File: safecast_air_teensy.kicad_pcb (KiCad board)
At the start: 2 copper layers, 108 x 69.8 mm, 47 parts, among them P1 CONN_5X2, P10 CONN_5_MOD, P2 CONN_5X2, P3 CONN_5X2, P4 CONN_2X2, P5 CONN_2, P6 CONN_2, P7 CONN_2, P8 CONN_2, P9 CONN_2, U1 GPS, U2 XBEE, U3 LCD, U4 OPENLOG, U5 POLOLU_3V3, U6 TEENSY3.1, U7 R5_BUSSED

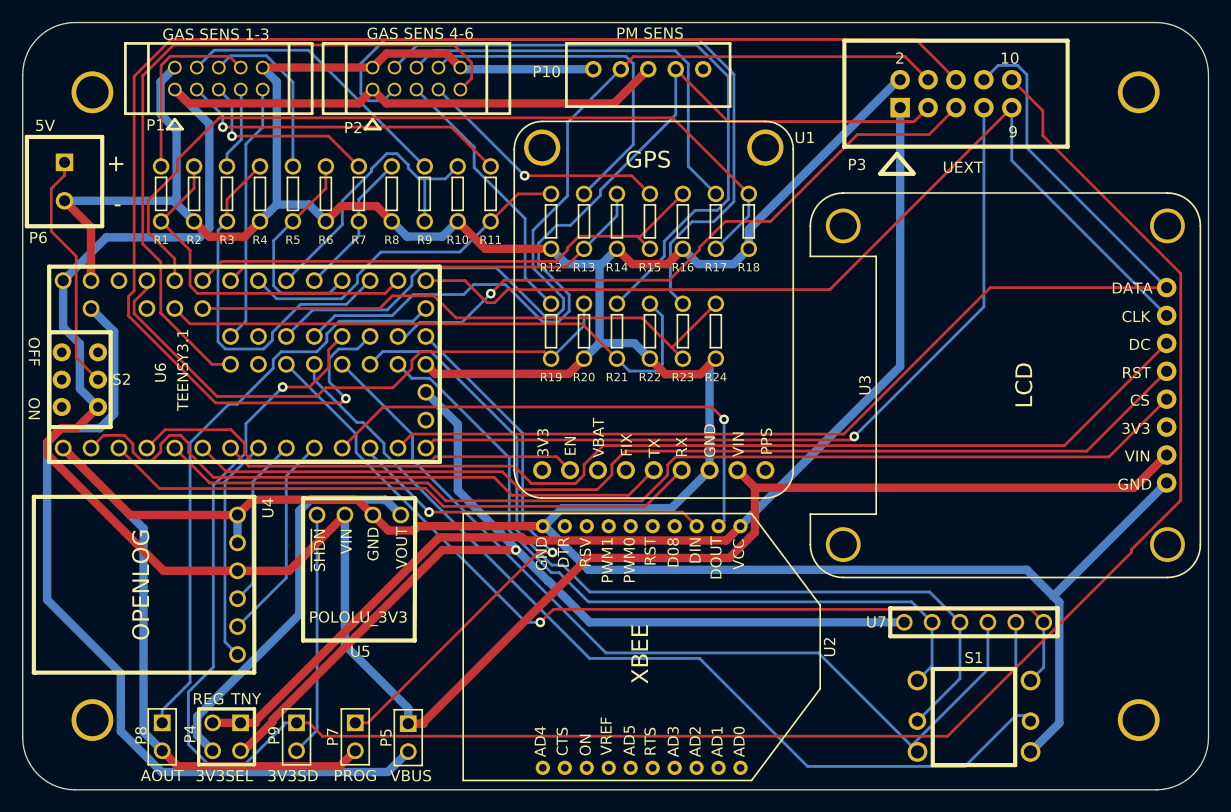
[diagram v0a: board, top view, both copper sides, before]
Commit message: Added pullup resistor to pwm1 and pwm2 signals from particulate sensor.
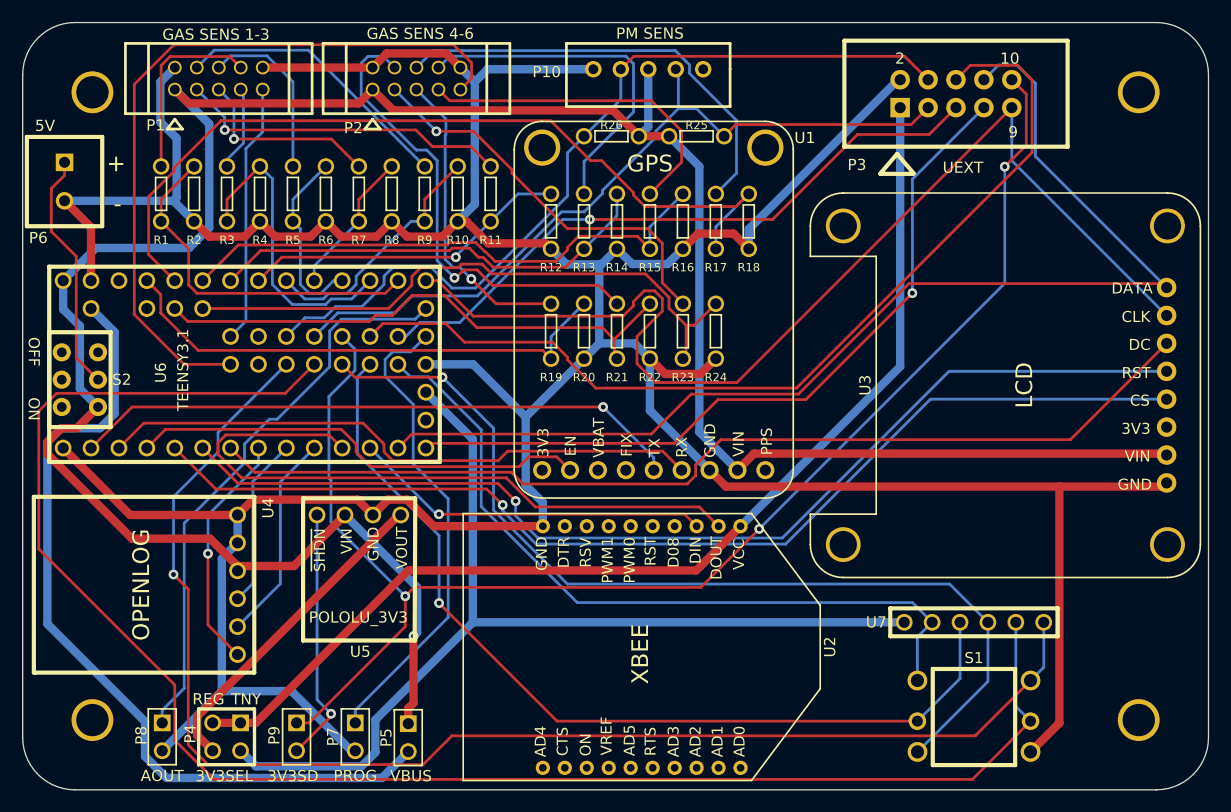
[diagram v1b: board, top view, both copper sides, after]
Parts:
- added R25: 10k, R_SMALL, F.Cu at (86.8, 35.8)
- added R26: 10k, R_SMALL, F.Cu at (79.0, 35.8)
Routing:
- net /JOY_D: track 92.3 -> 153.1 mm
- net /D31: track 191.3 -> 130.6 mm, vias 1 -> 3
- net /SDA: track 131.8 -> 86.8 mm, vias 1 -> 0
- net /JOY_CENT: track 86.4 -> 125.8 mm
- net /AUX6: track 67.6 -> 36.6 mm, vias 0 -> 1
- net GND: track 403.6 -> 378.9 mm
- net /SCK: track 86.3 -> 101.2 mm
- net /WRK6: track 58.5 -> 43.7 mm, vias 0 -> 1
- net /XBEE_DOUT: track 46.7 -> 61.4 mm, vias 1 -> 0
- net /PWM1: track 81.5 -> 70.8 mm
- net /PWM2: track 86.0 -> 75.8 mm
- net /AUX4: track 23.2 -> 30.6 mm, vias 1 -> 0
- net /3V3_REG: track 36.5 -> 29.8 mm
- net /AUX1_DIV: track 34.6 -> 28.0 mm
- net /AUX5_DIV: track 53.2 -> 47.0 mm
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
